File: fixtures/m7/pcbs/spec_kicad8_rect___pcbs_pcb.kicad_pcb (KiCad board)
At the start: 2 copper layers, 1 part

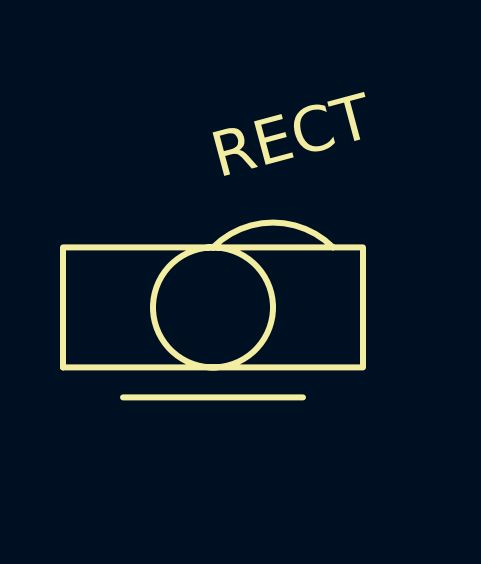
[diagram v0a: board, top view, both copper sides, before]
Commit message: Expand footprint specs and add JS footprints plan
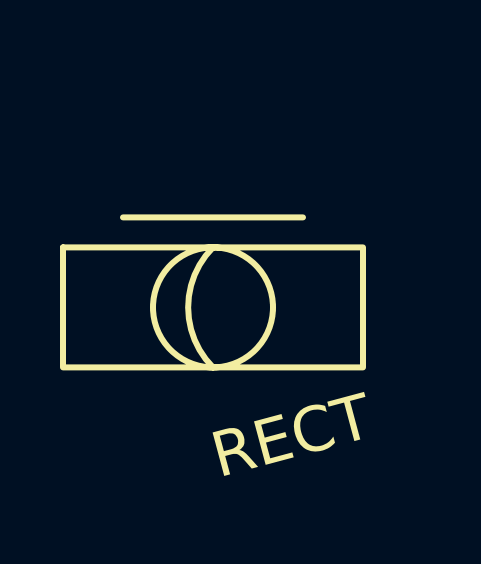
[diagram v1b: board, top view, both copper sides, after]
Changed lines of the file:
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@@
             (fp_text value "" (at 0 0) (layer F.SilkS) hide (effects (font (size 1.27 1.27) (thickness 0.15))))
             (fp_circle (center 0 0) (end 2 0) (layer F.SilkS) (width 0.2))
-            (fp_line (start -3 3) (end 3 3) (layer F.SilkS) (width 0.2))
-            (fp_arc (start 2 0) (end 0 -2) (angle 90) (layer F.SilkS) (width 0.2))
-            (fp_rect (start -5 2) (end 5 -2) (layer F.SilkS) (width 0.2))
-            (fp_text user "RECT" (at 0 -5 15) (layer F.SilkS) (effects (font (size 1.5 1.5) (thickness 0.2)) (justify left)))
+            (fp_line (start -3 -3) (end 3 -3) (layer F.SilkS) (width 0.2))
+            (fp_arc (start 2 0) (end 0 2) (angle 90) (layer F.SilkS) (width 0.2))
+            (fp_rect (start -5 -2) (end 5 2) (layer F.SilkS) (width 0.2))
+            (fp_text user "RECT" (at 0 5 15) (layer F.SilkS) (effects (font (size 1.5 1.5) (thickness 0.2)) (justify left)))
         )
 )
